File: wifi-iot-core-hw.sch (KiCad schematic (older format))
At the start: 48 parts, among them P1 USB, P10 CONN_01X01, P11 CONN_01X01, P3 CONN_01X16, P4 CONN_01X04, P5 CONN_01X16, P6 CONN_01X03, P7 CONN_01X03, P8 CONN_01X01, P9 CONN_01X01, SW1 RST, SW2 SW_PUSH_SMALL_H, U1 LP2985LV, U2 STM32F103C8Tx, U3 ESP-07v2, Y1 8MHz

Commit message: Fix Schematic & PCB
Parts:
- removed P3, P5: CONN_01X16, Pin_Headers:Pin_Header_Straight_1x16, symbol CONN_01X16
- removed P6, P7: CONN_01X03, Pin_Headers:Pin_Header_Straight_1x03, symbol CONN_01X03
- added C18: 100nF, lib:C_0603, symbol C_Small
- added C19: 15pF, lib:C_0603, symbol C_Small
- added C20: 15pf, lib:C_0603, symbol C_Small
- added P2, P3: CONN_01X20, Pin_Headers:Pin_Header_Straight_1x20, symbol CONN_01X20
- added Y2: 32.687, lib:crystal_smd_32.768_2Pin, symbol Crystal_Small
- C1, C10, C11, C12, C13, C14, C15, C16, C5, C6, C7, C8, C9: footprint Capacitors_SMD:C_0603 -> lib:C_0603
- C3: value 1uF -> 10nF; footprint Capacitors_SMD:C_0603 -> lib:C_0603
- P1: footprint w_conn_pc:conn_usb_B_micro_smd-2 -> lib:Micro_usb_B_smd
- P10, P11, P8, P9: footprint Mounting_Holes:MountingHole_3.5mm -> lib:MountingHole_2mm
- R1, R10, R11, R12, R13, R2, R3, R4, R5, R6, R7, R8, R9: footprint Resistors_SMD:R_0603 -> lib:R_0603
- SW1, SW2: footprint Buttons_Switches_SMD:SW_SPST_B3U-1000P-B -> lib:SW_SPST_B3U-1000P-B
- U2: footprint Housings_QFP:LQFP-48_7x7mm_Pitch0.5mm -> lib:LQFP-48_Pin1.7x0.3mm_Pitch0.5mm
- U3: footprint ESP8266:ESP-07v2-smd-16pin -> lib:ESP-07v2-smd-16pin
- Y1: footprint Crystal:HC49_sm -> lib:Crystal_SMD_5032_4Pads
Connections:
- net PA13 is gone; now on net USB_DIS: U2.2 (PC13/RTC_OUT/RTC_TAMPER)
- net PA8 is gone; now on net GPIO16: U2.29 (RCC_MCO/TIM1_CH1/USART1_CK/PA8)
- net PA9 is gone; now on net ESP_RXD: U2.30 (TIM1_CH2/USART1_TX/PA9)
- net +3V3: now also P2.1 (P1), P3.1 (P1), P3.19 (P19)
- net +5V: now also P2.20 (P20)
- net BUTTON: now also P3.20 (P20)
- net ESP_RXD: now also P3.4 (P4); no longer U2.42 (PB6/I2C1_SCL/TIM4_CH1/USART1_TX)
- net ESP_TXD: now also U2.31 (TIM1_CH3/USART1_RX/PA10), P3.3 (P3); no longer U2.43 (PB7/I2C1_SDA/TIM4_CH2/USART1_RX)
- net GNDREF: now also C18.1, C19.2, C20.2, P2.19 (P19), P2.3 (P3), P2.4 (P4), P3.17 (P17), P3.18 (P18), P3.2 (P2)
- net GPIO16: no longer U2.22 (PB11/ADC1_EXTI11/ADC2_EXTI11/I2C2_SDA/TIM2_CH4/USART3_RX)
- net PA0: now also P2.8 (P8)
- net PA1: now also P2.9 (P9)
- net PA2: now also P2.10 (P10)
- net PA3: now also P2.11 (P11)
- net PA4: now also P2.12 (P12)
- net PA5: now also P2.13 (P13)
- net PA6: now also P2.14 (P14)
- net PA7: now also P2.15 (P15)
- net PB10: now also P2.17 (P17)
- net PB12: now also P3.16 (P16)
- net PB13: now also P3.15 (P15)
- net PB14: now also P3.14 (P14)
- net PB15: now also P3.13 (P13)
- net PB2: now also P2.16 (P16)
- net PB3: now also P3.12 (P12)
- net PB4: now also P3.11 (P11)
- net PB5: now also P3.10 (P10)
- net PB8: now also P3.7 (P7)
- net PB9: now also P3.6 (P6)
- net USB_DIS: no longer U2.31 (TIM1_CH3/USART1_RX/PA10)
- net VBAT: now also C18.2, P2.2 (P2)
- net GPIO13: now reaches U3.7 (GPIO13)
- net GPIO13: now also P2.7 (P7)
- net GPIO12: now reaches U3.6 (GPIO12)
- net GPIO12: now also P2.6 (P6)
- net GPIO14: now reaches U3.5 (GPIO14)
- net GPIO14: now also P2.5 (P5)
- net ESP_PRO renamed PRO
- net PRO: now also P3.5 (P5)
- net OSC_IN: no longer names the net of C14.1, U2.5 (PD0/RCC_OSC_IN), Y1.1
- net OSC_OUT: no longer names the net of C15.1, U2.6 (PD1/RCC_OSC_OUT), Y1.2
- net PA14: no longer names the net of U2.3 (PC14/RCC_OSC32_IN)
- net PA14: now also C19.1, Y2.1
- net PA15: no longer names the net of U2.4 (PC15/ADC1_EXTI15/ADC2_EXTI15/RCC_OSC32_OUT)
- net PA15: now also C20.1, Y2.2
- new net PB11: P2.18 (P18), U2.22 (PB11/ADC1_EXTI11/ADC2_EXTI11/I2C2_SDA/TIM2_CH4/USART3_RX)
- new net PB6: P3.9 (P9), U2.42 (PB6/I2C1_SCL/TIM4_CH1/USART1_TX)
- new net PB7: P3.8 (P8), U2.43 (PB7/I2C1_SDA/TIM4_CH2/USART1_RX)
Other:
- moved on the sheet: C14, C15, P10, P11, P4, P8, P9, R1, U2, Y1

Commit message: Fix schematic & PCB
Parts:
- removed R10, R13: 10K, lib:R_0603, symbol R_Small
- added C8: 470pF, lib:C_0603, symbol C_Small
- added R6, R7: 10k, lib:R_0603, symbol R_Small
- D1: value Led PWR -> Led GPIO16
- renumbered C16 to C1, C11 to C10, C12 to C11, C13 to C12, C2 to C13, C4 to C14, C5 to C15, C6 to C16, C8 to C17, C9 to C18, C10 to C19, C17 to C2, C1 to C20, C3 to C21, C18 to C3, C14 to C4, C15 to C5, C19 to C6, C20 to C7, C7 to C9, P2 to P1, P3 to P2, P8 to P3, P9 to P4, P10 to P5, P11 to P6, P4 to P7, P1 to P8, R3 to R10, R4 to R11, R2 to R12, R6 to R13, R12 to R2, R11 to R3, R7 to R4, R9 to R5, R5 to R8, R8 to R9, U3 to U1, U1 to U3
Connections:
- net +3V3: now also P2.20 (P20), R8.1, R6.1, R7.1
- net GNDREF: now also C8.2; no longer D1.1 (K)
- net GPIO16: now also D1.1 (K)
- net CH_PD: now reaches U1.3 (CH_PD)
- net CH_PD: now also U2.19 (PB1/ADC1_IN9/ADC2_IN9/TIM1_CH3N/TIM3_CH4), R6.2
- net BUTTON renamed ESP_PRO
- net ESP_PRO: now also P2.5 (P5), U1.12 (GPIO0), C8.1, R7.2; no longer P2.20 (P20)
- removed net Led_u: R8.1, U2.19 (PB1/ADC1_IN9/ADC2_IN9/TIM1_CH3N/TIM3_CH4)
- net NRST renamed RST
- net RST: no longer U1.1 (REST)
- removed net PRO: P2.5 (P5), U1.12 (GPIO0), U2.18 (PB0/ADC1_IN8/ADC2_IN8/TIM1_CH2N/TIM3_CH3)
- new net ESP_RST: U1.1 (REST), U2.18 (PB0/ADC1_IN8/ADC2_IN8/TIM1_CH2N/TIM3_CH3)
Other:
- moved on the sheet: C1, C10, C11, C12, C2, C9, D1, P3, P4, P5, P6, P7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

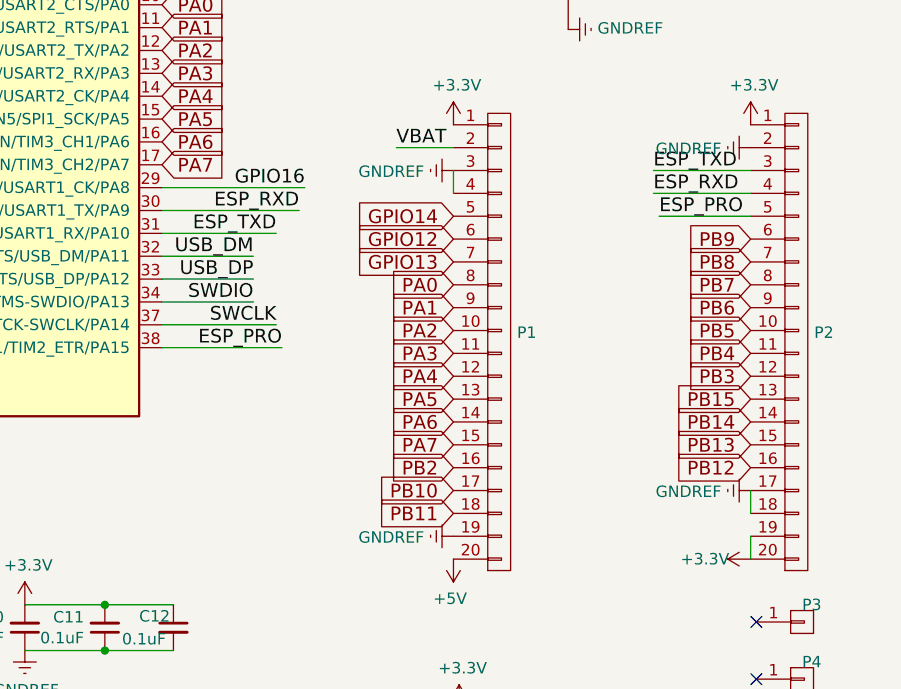
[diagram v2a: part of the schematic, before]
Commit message: Drop pin GPIO16 at pin STM32, add address support in PCB & size PCB 2,3x1,25 inch (5,8x3,2 mm)
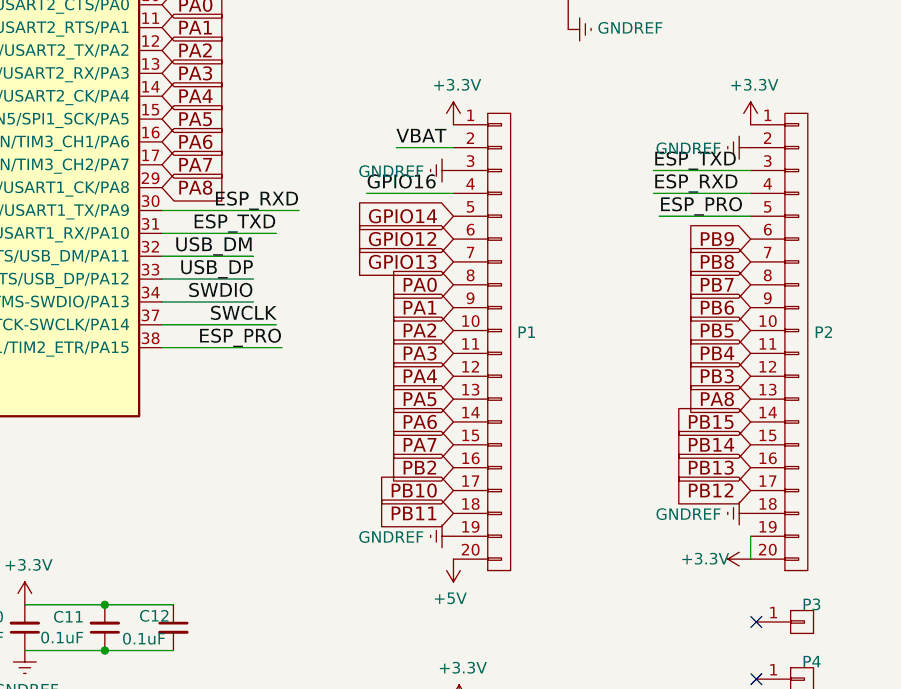
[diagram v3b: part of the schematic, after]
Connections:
- net GNDREF: no longer P1.4 (P4), P2.17 (P17)
- net GPIO16: now also P1.4 (P4); no longer U2.29 (RCC_MCO/TIM1_CH1/USART1_CK/PA8)
- net PB12: now also P2.17 (P17); no longer P2.16 (P16)
- net PB13: now also P2.16 (P16); no longer P2.15 (P15)
- net PB14: now also P2.15 (P15); no longer P2.14 (P14)
- net PB15: now also P2.14 (P14); no longer P2.13 (P13)
- new net PA8: P2.13 (P13), U2.29 (RCC_MCO/TIM1_CH1/USART1_CK/PA8)
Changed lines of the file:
@@
 Text GLabel 8850 4700 0    60   Input ~ 0
 PB10
+Text GLabel 10150 4700 0    60   Input ~ 0
+PB12
 Text GLabel 10150 4600 0    60   Input ~ 0
-PB12
+PB13
 Text GLabel 10150 4500 0    60   Input ~ 0
-PB13
+PB14
 Text GLabel 10150 4400 0    60   Input ~ 0
-PB14
-Text GLabel 10150 4300 0    60   Input ~ 0
 PB15
 Text GLabel 10150 4200 0    60   Input ~ 0
@@
 L GNDREF #PWR037
 U 1 1 57B64043
-P 10150 4700
-F 0 "#PWR037" H 10150 4450 50  0001 C CNN
-F 1 "GNDREF" V 10155 4572 50  0000 R CNN
-F 2 "" H 10150 4700 50  0000 C CNN
-F 3 "" H 10150 4700 50  0000 C CNN
-	1    10150 4700
+P 10150 4800
+F 0 "#PWR037" H 10150 4550 50  0001 C CNN
+F 1 "GNDREF" V 10155 4672 50  0000 R CNN
+F 2 "" H 10150 4800 50  0000 C CNN
+F 3 "" H 10150 4800 50  0000 C CNN
+	1    10150 4800
 	0    1    1    0
 $EndComp
@@
 	9725 3300 10150 3300
 Wire Wire Line
-	8850 3400 8850 3300
-Wire Wire Line
 	1000 1875 825  1875
 Wire Wire Line
@@
 GPIO16
 Wire Wire Line
-	7575 3375 8200 3375
-Text Label 8200 3375 2    60   ~ 0
-GPIO16
-Wire Wire Line
 	8452 1783 8052 1783
 Text Label 8052 1783 0    60   ~ 0
 GPIO16
-Wire Wire Line
-	10150 4800 10150 4700
 Wire Wire Line
 	10150 4900 10150 5000
@@
 	2450 5200 2450 5175
 Connection ~ 2450 5175
+Text GLabel 7575 3375 2    60   Input ~ 0
+PA8
+Text GLabel 10150 4300 0    60   Input ~ 0
+PA8
+Wire Wire Line
+	8850 3400 8470 3400
+Text Label 8470 3400 0    60   ~ 0
+GPIO16
 $EndSCHEMATC

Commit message: Fix assets file
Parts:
- renumbered SW2 to PRO, SW1 to RST
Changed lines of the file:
@@
 $EndComp
 $Comp
-L SW_PUSH_SMALL_H SW1
+L SW_PUSH_SMALL_H RST
 U 1 1 5791DC4D
 P 1750 5325
-F 0 "SW1" V 1750 5412 50  0000 L CNN
+F 0 "RST" V 1750 5412 50  0000 L CNN
 F 1 "RST" V 1795 5412 50  0001 L CNN
 F 2 "lib:SW_SPST_B3U-1000P-B" H 1750 5525 50  0001 C CNN
@@
 $EndComp
 $Comp
-L SW_PUSH_SMALL_H SW2
+L SW_PUSH_SMALL_H PRO
 U 1 1 5791DC0D
 P 2675 5325
-F 0 "SW2" V 2675 5412 50  0000 L CNN
+F 0 "PRO" V 2675 5412 50  0000 L CNN
 F 1 "SW_PUSH_SMALL_H" V 2720 5412 50  0001 L CNN
 F 2 "lib:SW_SPST_B3U-1000P-B" H 2675 5525 50  0001 C CNN
